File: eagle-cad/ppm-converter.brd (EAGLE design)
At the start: 49.5 x 49.5 mm, 18 parts, among them IC1 74HC14, IC2 74HC14, U1 ATMEGA328P, Y1 16Mhz

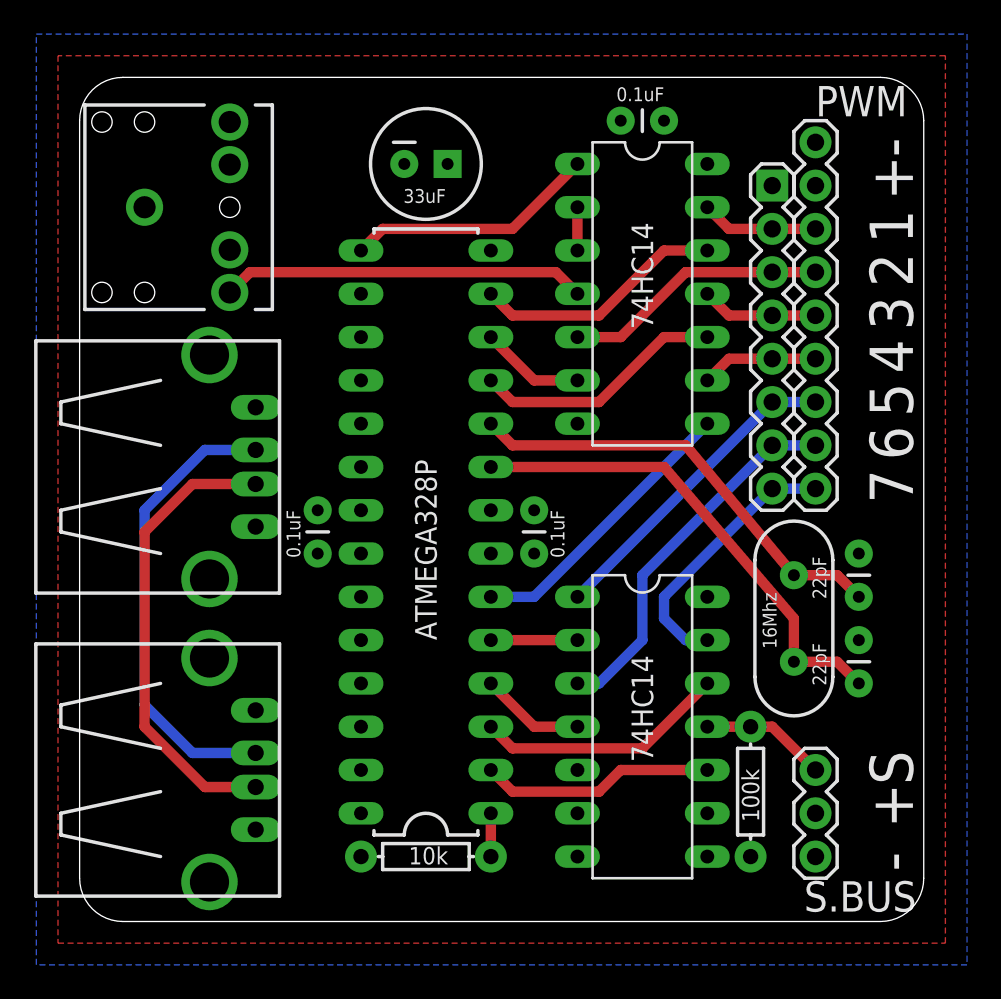
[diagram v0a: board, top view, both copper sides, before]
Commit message: Swapped pin texts to other side for better readibility
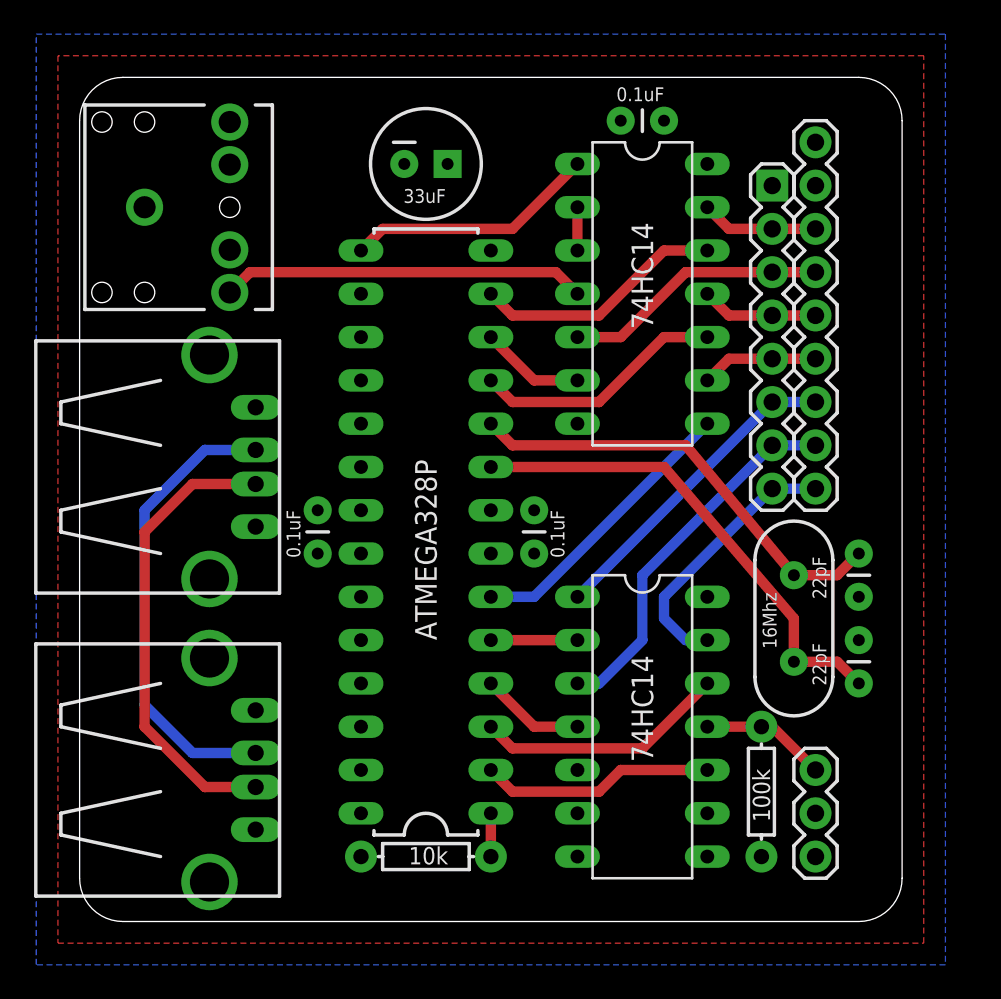
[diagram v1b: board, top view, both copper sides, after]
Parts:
- moved C3 2.54 mm to (45.7, 21.6), turned to 270 degrees
- moved R2 0.64 mm to (40.0, 7.62)
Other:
- board size 49.5 x 49.5 mm -> 48.3 x 49.5 mm
- board text added: "PWM/S.Bus to PPM -converter"
- board text added: "S.Bus"
- board text removed: "PWM/S.BUS to PPM -converter"
- board text removed: "S.BUS"
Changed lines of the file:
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@@
 <board>
 <plain>
-<text x="48.895" y="2.9464" size="2.54" layer="21" rot="R90">-</text>
-<text x="48.895" y="5.4864" size="2.54" layer="21" rot="R90">+</text>
-<text x="48.895" y="39.7764" size="2.54" layer="21" rot="R90">1</text>
-<text x="48.895" y="37.2364" size="2.54" layer="21" rot="R90">2</text>
-<text x="48.895" y="34.6964" size="2.54" layer="21" rot="R90">3</text>
-<text x="48.895" y="32.1564" size="2.54" layer="21" rot="R90">4</text>
-<text x="48.895" y="29.6164" size="2.54" layer="21" rot="R90">5</text>
-<text x="48.895" y="27.0764" size="2.54" layer="21" rot="R90">6</text>
-<text x="48.895" y="24.5364" size="2.54" layer="21" rot="R90">7</text>
-<text x="48.895" y="8.0264" size="2.54" layer="21" rot="R90">S</text>
-<text x="48.895" y="42.3164" size="2.54" layer="21" rot="R90">+</text>
-<text x="48.895" y="44.8564" size="2.54" layer="21" rot="R90">-</text>
-<text x="43.18" y="47.244" size="1.778" layer="25">PWM</text>
-<text x="49.0982" y="2.3622" size="1.778" layer="25" rot="R180">S.BUS</text>
-<text x="32.385" y="3.556" size="1.778" layer="26" rot="MR90">PWM/S.BUS to PPM -converter</text>
+<text x="45.085" y="2.9464" size="2.54" layer="22" rot="MR90">-</text>
+<text x="45.085" y="5.4864" size="2.54" layer="22" rot="MR90">+</text>
+<text x="45.085" y="39.7764" size="2.54" layer="22" rot="MR90">1</text>
+<text x="45.085" y="37.2364" size="2.54" layer="22" rot="MR90">2</text>
+<text x="45.085" y="34.6964" size="2.54" layer="22" rot="MR90">3</text>
+<text x="45.085" y="32.1564" size="2.54" layer="22" rot="MR90">4</text>
+<text x="45.085" y="29.6164" size="2.54" layer="22" rot="MR90">5</text>
+<text x="45.085" y="27.0764" size="2.54" layer="22" rot="MR90">6</text>
+<text x="45.085" y="24.5364" size="2.54" layer="22" rot="MR90">7</text>
+<text x="45.085" y="8.0264" size="2.54" layer="22" rot="MR90">S</text>
+<text x="45.085" y="42.3164" size="2.54" layer="22" rot="MR90">+</text>
+<text x="45.085" y="44.8564" size="2.54" layer="22" rot="MR90">-</text>
+<text x="45.72" y="47.244" size="1.778" layer="26" rot="MR0">PWM</text>
+<text x="40.2082" y="2.3622" size="1.778" layer="26" rot="MR180">S.Bus</text>
+<text x="32.385" y="3.556" size="1.778" layer="26" rot="MR90">PWM/S.Bus to PPM -converter</text>
 <text x="19.558" y="9.398" size="1.778" layer="26" rot="MR90">Pertti Erkkilä 2013</text>
-<wire x1="2.54" y1="0" x2="46.99" y2="0" width="0" layer="20"/>
-<wire x1="49.53" y1="2.54" x2="49.53" y2="46.99" width="0" layer="20"/>
-<wire x1="46.99" y1="49.53" x2="2.54" y2="49.53" width="0" layer="20"/>
+<wire x1="2.54" y1="0" x2="45.72" y2="0" width="0" layer="20"/>
+<wire x1="48.26" y1="2.54" x2="48.26" y2="46.99" width="0" layer="20"/>
+<wire x1="45.72" y1="49.53" x2="2.54" y2="49.53" width="0" layer="20"/>
 <wire x1="0" y1="46.99" x2="0" y2="2.54" width="0" layer="20"/>
 <wire x1="0" y1="46.99" x2="2.54" y2="49.53" width="0" layer="20" curve="-90"/>
-<wire x1="46.99" y1="49.53" x2="49.53" y2="46.99" width="0" layer="20" curve="-90"/>
-<wire x1="49.53" y1="2.54" x2="46.99" y2="0" width="0" layer="20" curve="-90"/>
+<wire x1="45.72" y1="49.53" x2="48.26" y2="46.99" width="0" layer="20" curve="-90"/>
+<wire x1="48.26" y1="2.54" x2="45.72" y2="0" width="0" layer="20" curve="-90"/>
 <wire x1="2.54" y1="0" x2="0" y2="2.54" width="0" layer="20" curve="-90"/>
 </plain>
@@
 <attribute name="VALUE" x="40.894" y="16.002" size="0.8128" layer="25" ratio="10" rot="R90"/>
 </element>
-<element name="C3" library="SparkFun-Passives" package="CAP-PTH-SMALL" value="22pF" x="45.72" y="19.05" smashed="yes" rot="R90">
+<element name="C3" library="SparkFun-Passives" package="CAP-PTH-SMALL" value="22pF" x="45.72" y="21.59" smashed="yes" rot="R270">
 <attribute name="VALUE" x="43.815" y="18.923" size="0.8128" layer="25" rot="R90"/>
 </element>
@@
 </element>
 <element name="JP1" library="SparkFun-Connectors" package="1X08" value="" x="40.64" y="43.18" smashed="yes" rot="R270"/>
-<element name="R2" library="SparkFun-Passives" package="AXIAL-0.3" value="100k" x="39.37" y="7.62" smashed="yes" rot="R270">
-<attribute name="VALUE" x="39.878" y="5.842" size="1.016" layer="21" font="vector" ratio="15" rot="R90"/>
+<element name="R2" library="SparkFun-Passives" package="AXIAL-0.3" value="100k" x="40.005" y="7.62" smashed="yes" rot="R270">
+<attribute name="VALUE" x="40.513" y="5.842" size="1.016" layer="21" font="vector" ratio="15" rot="R90"/>
 </element>
 </elements>
@@
 <polygon width="0.6096" layer="16" isolate="0.4064">
 <vertex x="-2.54" y="52.07"/>
-<vertex x="52.07" y="52.07"/>
-<vertex x="52.07" y="-2.54"/>
+<vertex x="50.8" y="52.07"/>
+<vertex x="50.8" y="-2.54"/>
 <vertex x="-2.54" y="-2.54"/>
 </polygon>
@@
 <wire x1="35.56" y1="27.94" x2="41.91" y2="20.32" width="0.6096" layer="1"/>
 <wire x1="41.91" y1="20.32" x2="44.45" y2="20.32" width="0.6096" layer="1"/>
-<wire x1="44.45" y1="20.32" x2="45.72" y2="19.05" width="0.6096" layer="1"/>
 <wire x1="25.4" y1="27.94" x2="24.13" y2="29.21" width="0.6096" layer="1"/>
+<wire x1="44.45" y1="20.32" x2="45.72" y2="21.59" width="0.6096" layer="1"/>
 </signal>
 <signal name="N$6">
@@
 <contactref element="R2" pad="P$1"/>
 <contactref element="IC2" pad="11"/>
-<wire x1="43.18" y1="8.89" x2="40.64" y2="11.43" width="0.6096" layer="1"/>
-<wire x1="40.64" y1="11.43" x2="39.37" y2="11.43" width="0.6096" layer="1"/>
-<wire x1="39.37" y1="11.43" x2="36.83" y2="11.43" width="0.6096" layer="1"/>
+<wire x1="40.005" y1="11.43" x2="36.83" y2="11.43" width="0.6096" layer="1"/>
+<wire x1="40.005" y1="11.43" x2="40.64" y2="11.43" width="0.6096" layer="1"/>
+<wire x1="40.64" y1="11.43" x2="43.18" y2="8.89" width="0.6096" layer="1"/>
 </signal>
 <signal name="N$26">
@@
 <polygon width="0.6096" layer="1" isolate="0.4064">
 <vertex x="-1.27" y="-1.27"/>
-<vertex x="50.8" y="-1.27"/>
-<vertex x="50.8" y="50.8"/>
+<vertex x="49.53" y="-1.27"/>
+<vertex x="49.53" y="50.8"/>
 <vertex x="-1.27" y="50.8"/>
 </polygon>

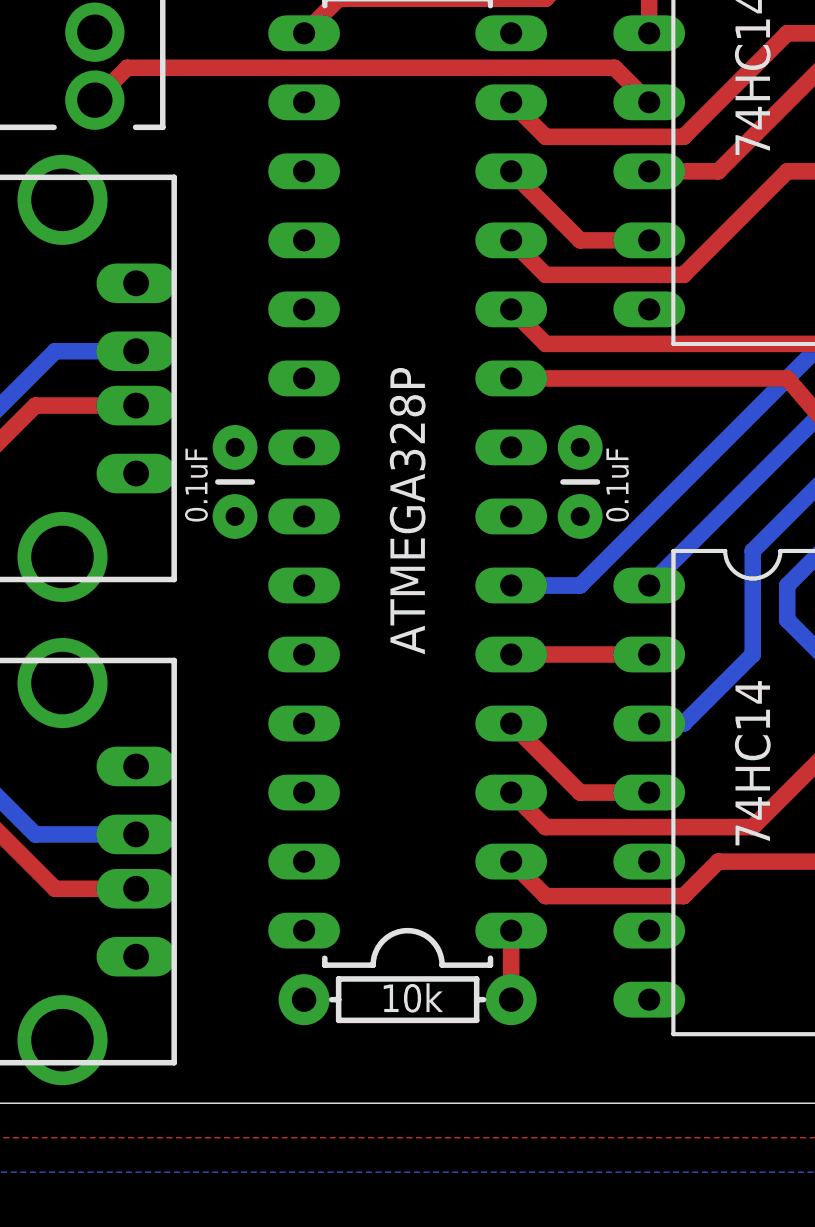
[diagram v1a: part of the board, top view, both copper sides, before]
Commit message: Added ISP-header
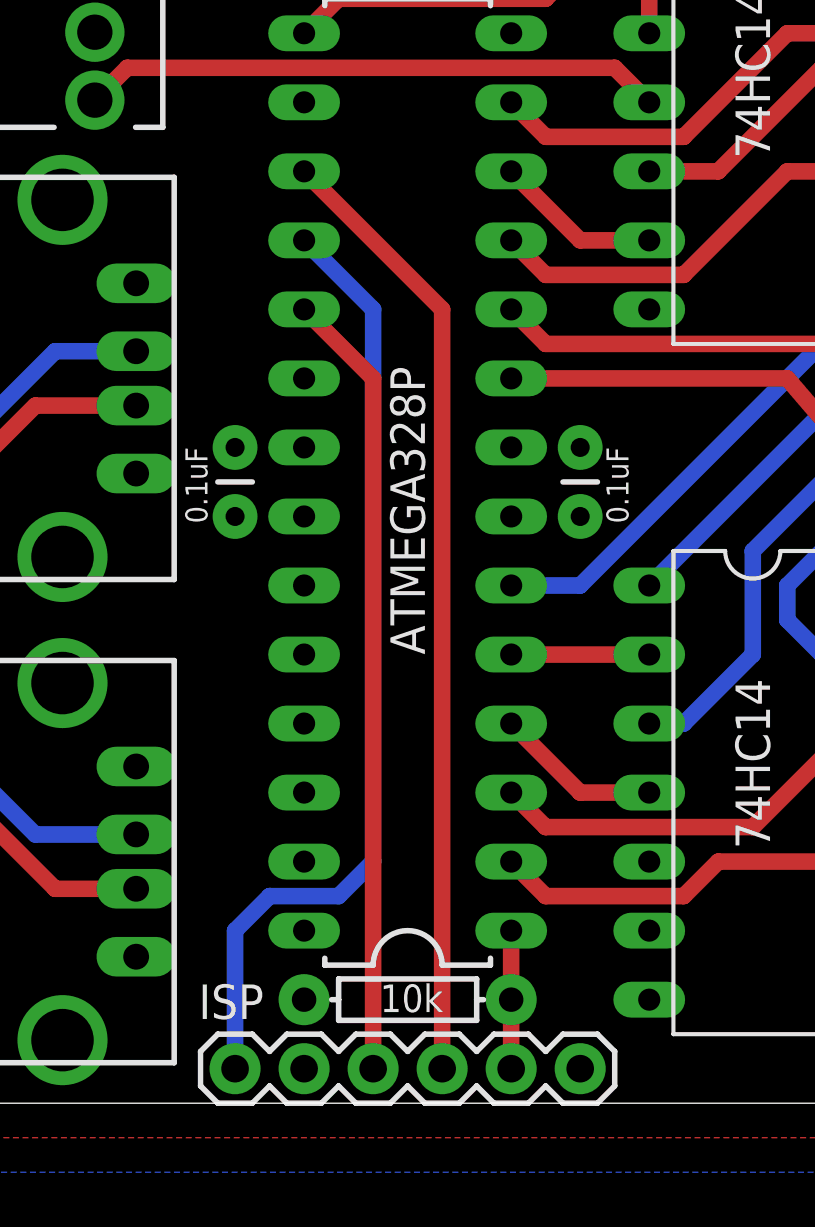
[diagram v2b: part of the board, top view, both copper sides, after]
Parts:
- added ISP: (no value), SparkFun-Connectors:1X06
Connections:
- new net N$18: ISP.1, U1.18
- new net N$28: ISP.3, U1.19
- new net N$29: ISP.4, U1.17
- net GND: now also ISP.6
- net N$4: now also ISP.5
- net VCC: now also ISP.2
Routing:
- net N$29: track 0.00 -> 35.1 mm
- net N$18: track 0.00 -> 35.1 mm
- net N$28: track 0.00 -> 29.0 mm
- net N$4: track 2.54 -> 5.08 mm
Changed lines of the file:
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@@
 <?xml version="1.0" encoding="utf-8"?>
 <!DOCTYPE eagle SYSTEM "eagle.dtd">
-<eagle version="6.3">
+<eagle version="6.4">
 <drawing>
 <settings>
@@
 <attribute name="VALUE" x="40.513" y="5.842" size="1.016" layer="21" font="vector" ratio="15" rot="R90"/>
 </element>
+<element name="ISP" library="SparkFun-Connectors" package="1X06" value="" x="13.97" y="1.27"/>
 </elements>
 <signals>
@@
 <contactref element="U2" pad="SLEEVE"/>
 <contactref element="IC2" pad="5"/>
+<contactref element="ISP" pad="6"/>
 </signal>
 <signal name="N$2">
@@
 <contactref element="U1" pad="1"/>
 <contactref element="R1" pad="P$1"/>
+<contactref element="ISP" pad="5"/>
 <wire x1="24.13" y1="6.35" x2="24.13" y2="3.81" width="0.6096" layer="1"/>
+<wire x1="24.13" y1="3.81" x2="24.13" y2="1.27" width="0.6096" layer="1"/>
 </signal>
 <signal name="N$5">
@@
 <contactref element="IC1" pad="14"/>
 <contactref element="IC2" pad="14"/>
+<contactref element="ISP" pad="2"/>
 </signal>
 <signal name="N$1">
@@
 <wire x1="29.21" y1="16.51" x2="24.13" y2="16.51" width="0.6096" layer="1"/>
 </signal>
+<signal name="N$18">
+<contactref element="U1" pad="18"/>
+<contactref element="ISP" pad="1"/>
+<wire x1="13.97" y1="1.27" x2="13.97" y2="6.35" width="0.6096" layer="16"/>
+<wire x1="13.97" y1="6.35" x2="15.24" y2="7.62" width="0.6096" layer="16"/>
+<wire x1="15.24" y1="7.62" x2="17.78" y2="7.62" width="0.6096" layer="16"/>
+<wire x1="17.78" y1="7.62" x2="19.05" y2="8.89" width="0.6096" layer="16"/>
+<wire x1="19.05" y1="8.89" x2="19.05" y2="29.21" width="0.6096" layer="16"/>
+<wire x1="19.05" y1="29.21" x2="16.51" y2="31.75" width="0.6096" layer="16"/>
+</signal>
+<signal name="N$28">
+<contactref element="U1" pad="19"/>
+<contactref element="ISP" pad="3"/>
+<wire x1="19.05" y1="1.27" x2="19.05" y2="26.67" width="0.6096" layer="1"/>
+<wire x1="19.05" y1="26.67" x2="16.51" y2="29.21" width="0.6096" layer="1"/>
+</signal>
+<signal name="N$29">
+<contactref element="U1" pad="17"/>
+<contactref element="ISP" pad="4"/>
+<wire x1="21.59" y1="1.27" x2="21.59" y2="29.21" width="0.6096" layer="1"/>
+<wire x1="21.59" y1="29.21" x2="16.51" y2="34.29" width="0.6096" layer="1"/>
+</signal>
 </signals>
